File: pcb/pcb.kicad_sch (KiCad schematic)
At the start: 7 parts

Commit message: Start schematic
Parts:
- removed C? (x2): 100n, Capacitor_SMD:C_0603_1608Metric, symbol Device:C
- removed C? (x2): 22u, Capacitor_SMD:CP_Elec_4x3.9, symbol Device:C_Polarized_Small
- removed J?: EURO_PWR_2x5, Connector_IDC:IDC-Header_2x05_P2.54mm_Vertical, symbol eurocad:EURO_PWR_2x5
- removed R? (x2): 22R, Resistor_SMD:R_0603_1608Metric, symbol Device:R
- added C10, C12, C4, C5, C9: 100n, Capacitor_SMD:C_0603_1608Metric, symbol Device:C
- added C11, C13, C2, C3, C6: 10u, Capacitor_SMD:C_0805_2012Metric, symbol Device:C
- added C14, C16: 1n, Capacitor_SMD:C_0603_1608Metric, symbol Device:C
- added C15, C17: 100p, Capacitor_SMD:C_0603_1608Metric, symbol Device:C
- added C7, C8: 2.2u, Capacitor_SMD:C_0805_2012Metric, symbol Device:C
- added D1, D2: 1N5819, Diode_SMD:D_SOD-123, symbol Diode:1N5819
- added D10, D11, D12, D13, D14, D15, D16, D17, D18, D3, D4, D5, D6, D7, D8, D9: BAT54J, Diode_SMD:D_SOD-323F, symbol Diode:BAT54J
- added FB1: BLM21PG600SN1D, Inductor_SMD:L_0805_2012Metric, symbol Device:FerriteBead
- added J1, J10, J11, J2, J3, J5, J6, J7, J8, J9: PJ301M-12, Eurocad:PJ301M-12, symbol eurocad:PJ301M-12
- added J4: EURO_PWR_2x5, Eurocad:Eurorack_Power_Header, symbol eurocad:EURO_PWR_2x5
- added R10, R12, R14, R16, R18, R20, R6, R8: 100K, Resistor_SMD:R_0603_1608Metric, symbol Device:R
- added R11, R13, R15, R17, R19, R21, R25, R29, R7, R9: 1K, Resistor_SMD:R_0603_1608Metric, symbol Device:R
- added R22, R26: 2K2, Resistor_SMD:R_0603_1608Metric, symbol Device:R
- added R23, R27: 10K, Resistor_SMD:R_0603_1608Metric, symbol Device:R
- added R24, R28: 33K, Resistor_SMD:R_0603_1608Metric, symbol Device:R
- added SW1: RotaryEncoder_Switch, Rotary_Encoder:RotaryEncoder_Bourns_Horizontal_PEC09-2xxxF-Nxxxx, symbol Device:RotaryEncoder_Switch
- added U1: PCM5102, Package_SO:TSSOP-20_4.4x6.5mm_P0.65mm, symbol Audio:PCM5102
- added U2: TL072, Package_SO:SOIC-8_3.9x4.9mm_P1.27mm, symbol Amplifier_Operational:TL072
- added U6: Pico, MCU_RaspberryPi_and_Boards:RPi_Pico_SMD_TH, symbol MCU_RaspberryPi_and_Boards:Pico
- added U7: AZ1117-5.0, Package_TO_SOT_SMD:SOT-223-3_TabPin2, symbol Regulator_Linear:AZ1117-5.0
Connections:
- net +12V: now also C2.1, C4.1, D1.1 (K), U2.8 (V+), U7.3 (VI)
- net -12V: now also C3.2, C5.2, D2.2 (A), U2.4 (V-)
- net GND: now also C10.2, C11.2, C12.2, C13.2, C14.2, C16.2, C2.2, C3.1, C4.2, C5.1, C6.2, C8.2, C9.2, D10.2 (A), D12.2 (A), D14.2 (A), D16.2 (A), D18.2 (A), D3.2 (A), D6.2 (A), D8.2 (A), J1.1, J10.1, J11.1, J2.1, J3.1, J4.3 (GND), J4.4 (GND), J4.5 (GND), J4.6 (GND), J4.7 (GND), J4.8 (GND), J5.1, J6.1, J7.1, J8.1, J9.1, R10.1, R12.1, R14.1, R16.1, R18.1, R20.1, R6.1, R8.1, U1.10 (DEMP), U1.11 (FLT), U1.12 (SCK), U1.16 (FMT), U1.19 (DGND), U1.3 (CPGND), U1.9 (AGND), U2.3 (+), U2.5 (+), U6.13 (GND), U6.18 (GND), U6.23 (GND), U6.28 (GND), U6.3 (GND), U6.33 (AGND), U6.38 (GND), U6.42 (GND), U6.8 (GND), U7.1 (GND)
- new net: J2.3, R8.2, R9.2
- new net: C7.1, U1.2 (CAPP)
- new net: C7.2, U1.4 (CAPM)
- new net: C10.1, C11.1, FB1.2, U1.1 (CPVDD), U1.8 (AVDD)
- new net: J8.3, R18.2, R19.2
- new net: J7.3, R16.2, R17.2
- new net: C17.1, R27.1, R28.2, U2.6 (-)
- new net: C17.2, R28.1, R29.2, U2.7
- new net: C9.1, U1.18 (LDOO)
- new net: C8.1, U1.5 (VNEG)
- new net: J6.3, R14.2, R15.2
- new net: J3.3, R10.2, R11.2
- new net: J9.3, R20.2, R21.2
- new net: D1.2 (A), J4.1 (+12V), J4.2 (+12V)
- new net: D2.1 (K), J4.10 (-12V), J4.9 (-12V)
- new net: J5.3, R12.2, R13.2
- new net: C15.2, R24.1, R25.2, U2.1
- new net: C15.1, R23.1, R24.2, U2.2 (-)
- new net: C14.1, R22.1, R23.2
- new net: J11.3, R29.1
- new net: J10.3, R25.1
- new net: C16.1, R26.1, R27.2
- new net: J1.3, R6.2, R7.2
- new net +3V3: C12.1, C13.1, D11.1 (K), D13.1 (K), D15.1 (K), D17.1 (K), D4.1 (K), D5.1 (K), D7.1 (K), D9.1 (K), FB1.1, U1.20 (DVDD), U6.36 (3V3)
- new net +5V: C6.1, U6.39 (VSYS), U7.2 (VO)
- new net GPIO26: U1.14 (DIN), U6.31 (GPIO26_ADC0)
- new net GPIO27: U1.13 (BCK), U6.32 (GPIO27_ADC1)
- new net GPIO28: U1.15 (LRCK), U6.34 (GPIO28_ADC2)
- new net L: R22.2, U1.6 (OUTL)
- new net R: R26.2, U1.7 (OUTR)
- new net TRIGGER 1: D3.1 (K), D4.2 (A), R7.1
- new net TRIGGER 2: D5.2 (A), D6.1 (K), R9.1
- new net TRIGGER 3: D7.2 (A), D8.1 (K), R11.1
- new net TRIGGER 4: D10.1 (K), D9.2 (A), R13.1
- new net TRIGGER 5: D11.2 (A), D12.1 (K), R15.1
- new net TRIGGER 6: D13.2 (A), D14.1 (K), R17.1
- new net TRIGGER 7: D15.2 (A), D16.1 (K), R19.1
- new net TRIGGER 8: D17.2 (A), D18.1 (K), R21.1
- no-connect marks 0 -> 10

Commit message: Continue schematic
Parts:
- added R30, R31, R32: 100K, Resistor_SMD:R_0603_1608Metric, symbol Device:R
- SW1: value RotaryEncoder_Switch -> Encoder
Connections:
- net +3V3: now also R30.2, R31.2, R32.2
- net GND: now also SW1.C, SW1.S2
- net GPIO26: no longer U1.14 (DIN)
- net GPIO27: no longer U1.13 (BCK)
- net GPIO28: now also SW1.S1, R30.1; no longer U1.15 (LRCK)
- net GPIO18: now reaches U6.24 (GPIO18)
- net GPIO18: now also SW1.A, R31.1
- net GPIO19: now reaches U6.25 (GPIO19)
- net GPIO19: now also SW1.B, R32.1
- net GPIO20: now reaches U6.26 (GPIO20)
- net GPIO20: now also U1.14 (DIN)
- net GPIO21: now reaches U6.27 (GPIO21)
- net GPIO21: now also U1.13 (BCK)
- net GPIO22: now reaches U6.29 (GPIO22)
- net GPIO22: now also U1.15 (LRCK)
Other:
- moved on the sheet: SW1

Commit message: Add LEDs, Triggers and CV in (closes #1)
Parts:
- added D19, D20, D21, D22, D23, D24, D25, D26: 3mm LED Com. Cath., LED_THT:LED_D3.0mm-3, symbol Device:LED_Dual_AKA
- added J12: PJ301M-12, Eurocad:PJ301M-12, symbol eurocad:PJ301M-12
- added Q1, Q2, Q3, Q4, Q5, Q6, Q7, Q8: MMBT3906, Package_TO_SOT_SMD:SOT-23, symbol Transistor_BJT:MMBT3906
- added R33, R36, R39, R40, R45, R46, R47, R48: 1K, Resistor_SMD:R_0603_1608Metric, symbol Device:R
- added R34, R35, R37, R38, R41, R42, R43, R44, R49, R50, R51, R52, R53, R54, R55, R56: 330R, Resistor_SMD:R_0603_1608Metric, symbol Device:R
- added R57, R59, R61: 100K, Resistor_SMD:R_0603_1608Metric, symbol Device:R
- added R58: 15K, Resistor_SMD:R_0603_1608Metric, symbol Device:R
- added R60: 12K, Resistor_SMD:R_0603_1608Metric, symbol Device:R
- added U3: MCP6002-xSN, Package_SO:SOIC-8_3.9x4.9mm_P1.27mm, symbol Amplifier_Operational:MCP6002-xSN
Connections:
- net +12V: now also U3.8 (V+)
- net +3V3: now also Q1.2 (E), Q2.2 (E), Q3.2 (E), Q4.2 (E), Q5.2 (E), Q6.2 (E), Q7.2 (E), Q8.2 (E)
- net -12V: now also R60.2, U3.4 (V-)
- net GND: now also D19.2 (K), D20.2 (K), D21.2 (K), D22.2 (K), D23.2 (K), D24.2 (K), D25.2 (K), D26.2 (K), J12.1, J12.2, R61.2, U3.3 (+), U3.5 (+)
- net TRIGGER 1: now also U6.1 (GPIO0)
- net TRIGGER 2: now also U6.4 (GPIO2)
- net TRIGGER 3: now also U6.6 (GPIO4)
- net TRIGGER 4: now also U6.9 (GPIO6)
- net TRIGGER 5: now also U6.11 (GPIO8)
- net TRIGGER 6: now also U6.14 (GPIO10)
- net TRIGGER 7: now also U6.16 (GPIO12)
- net TRIGGER 8: now also U6.19 (GPIO14)
- net LED 4: now reaches U6.10 (GPIO7)
- net LED 4: now also R39.2, R42.2
- net LED 5: now reaches U6.12 (GPIO9)
- net LED 5: now also R48.2, R56.2
- net LED 6: now reaches U6.15 (GPIO11)
- net LED 6: now also R47.2, R54.2
- net LED 7: now reaches U6.17 (GPIO13)
- net LED 7: now also R46.2, R52.2
- net LED 1: now reaches U6.2 (GPIO1)
- net LED 1: now also R33.2, R35.2
- net LED 8: now reaches U6.20 (GPIO15)
- net LED 8: now also R45.2, R50.2
- net LED 2: now reaches U6.5 (GPIO3)
- net LED 2: now also R36.2, R38.2
- net LED 3: now reaches U6.7 (GPIO5)
- net LED 3: now also R40.2, R44.2
- net GPIO26 renamed CV
- net CV: now also R58.1, U3.1
- net GPIO27: no longer names the net of U6.32 (GPIO27_ADC1)
- new net: D23.1 (A1), R50.1
- new net: D23.3 (A2), R49.2
- new net: Q3.1 (B), R39.1
- new net: Q3.3 (C), R41.1
- new net: Q1.3 (C), R34.1
- new net: D19.3 (A2), R34.2
- new net: Q8.1 (B), R48.1
- new net: D21.1 (A1), R42.1
- new net: D21.3 (A2), R41.2
- new net: Q6.1 (B), R46.1
- new net: Q6.3 (C), R51.1
- new net: D20.1 (A1), R38.1
- new net: D20.3 (A2), R37.2
- new net: D26.1 (A1), R56.1
- new net: Q8.3 (C), R55.1
- new net: D26.3 (A2), R55.2
- new net: D22.1 (A1), R44.1
- new net: D22.3 (A2), R43.2
- new net: Q1.1 (B), R33.1
- new net: Q5.3 (C), R49.1
- new net: D25.1 (A1), R54.1
- new net: D25.3 (A2), R53.2
- new net: U3.6 (-), U3.7
- new net: Q2.1 (B), R36.1
- new net: Q2.3 (C), R37.1
- new net: D24.1 (A1), R52.1
- new net: Q4.1 (B), R40.1
- new net: D19.1 (A1), R35.1
- new net: Q5.1 (B), R45.1
- new net: Q7.1 (B), R47.1
- new net: D24.3 (A2), R51.2
- new net: Q7.3 (C), R53.1
- new net: R57.1, R58.2, R59.1, U3.2 (-)
- new net: J12.3, R57.2
- new net: Q4.3 (C), R43.1
- new net -10V: R59.2, R60.1, R61.1
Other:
- moved on the sheet: C14, C15, C16, C17, C2, C3, C4, C5, C6, D1, D2, J10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

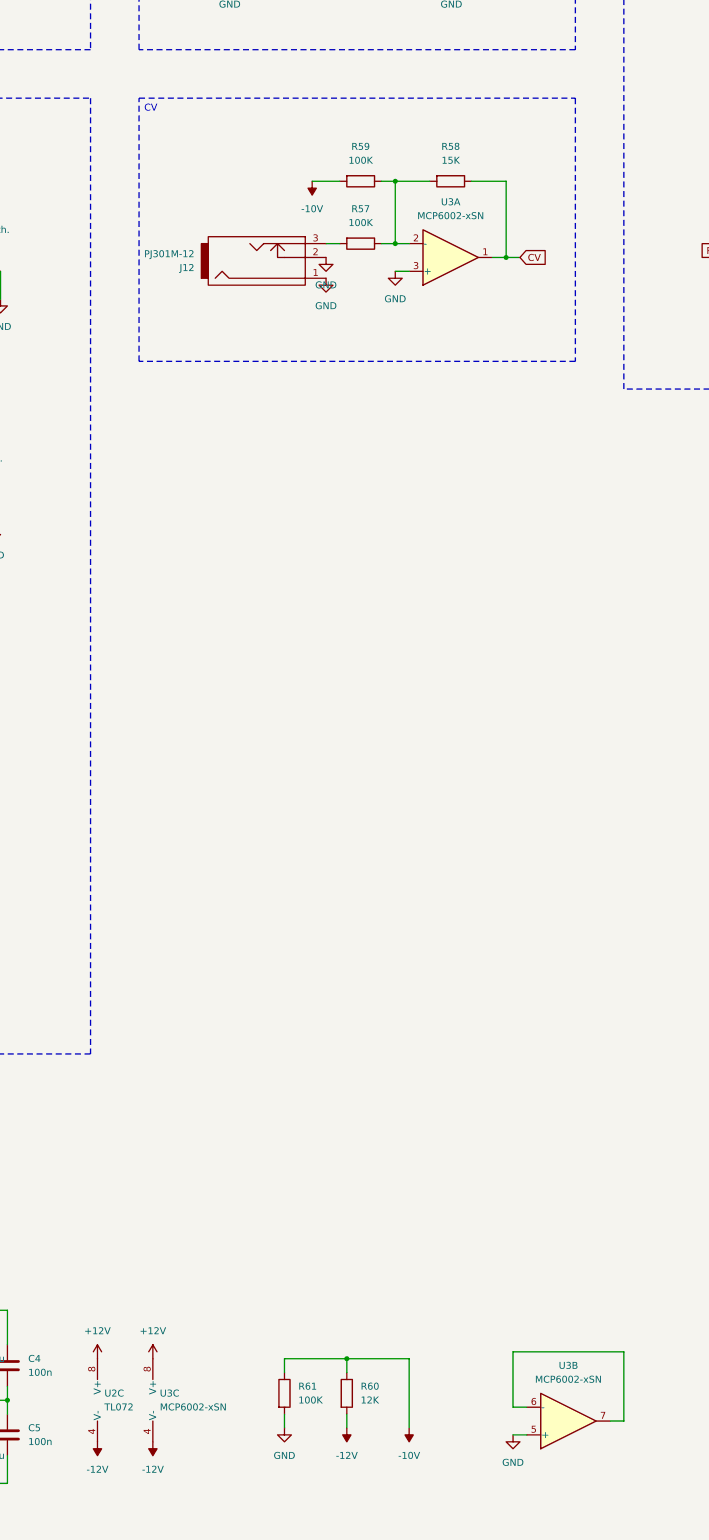
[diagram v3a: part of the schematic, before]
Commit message: Replace OP-Amp and add GPIO input protection diodes for eventual clamping
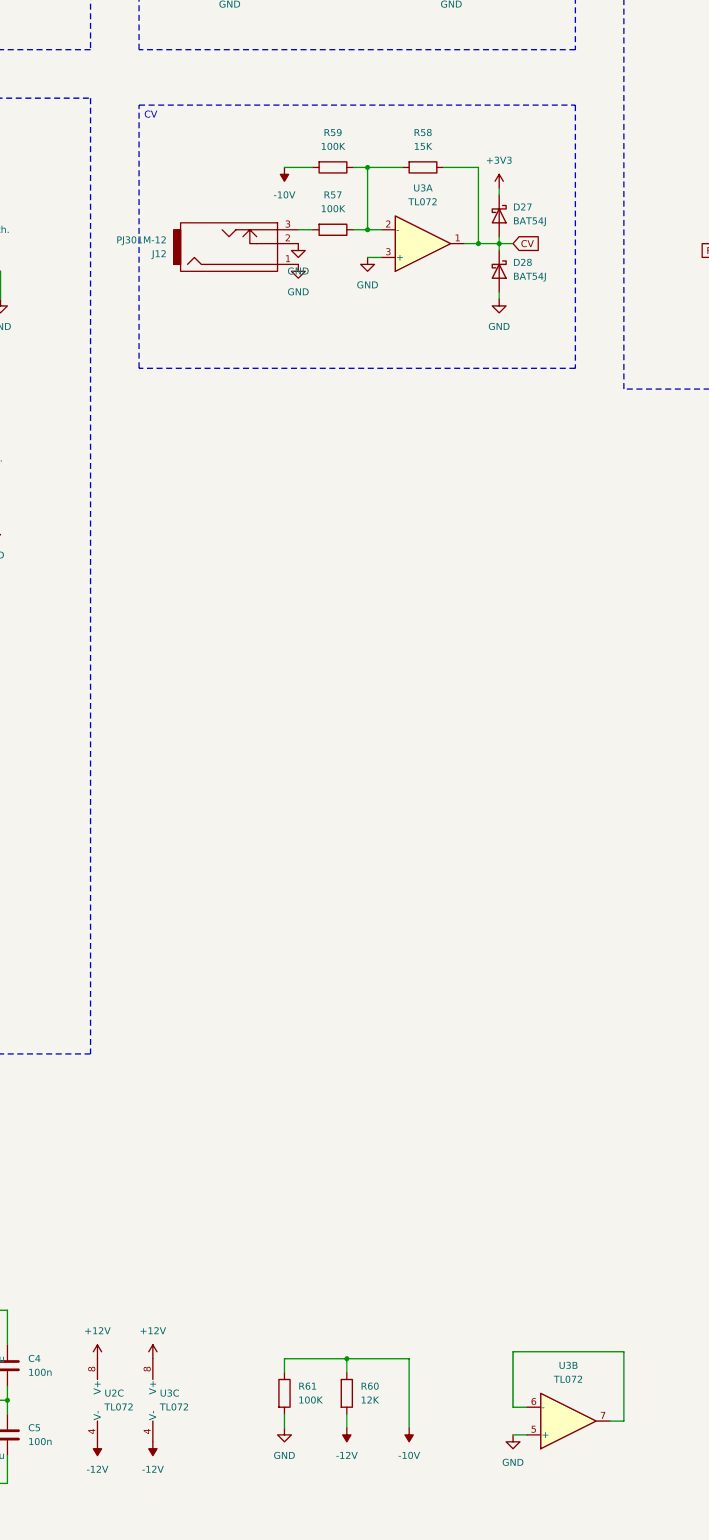
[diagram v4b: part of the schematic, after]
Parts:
- removed U3: MCP6002-xSN, Package_SO:SOIC-8_3.9x4.9mm_P1.27mm, symbol Amplifier_Operational:MCP6002-xSN
- added D27, D28: BAT54J, Diode_SMD:D_SOD-323F, symbol Diode:BAT54J
- added U3: TL072, Package_SO:SOIC-8_3.9x4.9mm_P1.27mm, symbol Amplifier_Operational:TL072
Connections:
- net +12V: now also U3.8 (V+)
- net +3V3: now also D27.1 (K)
- net -12V: now also U3.4 (V-)
- net CV: now also D27.2 (A), D28.1 (K), U3.1
- net GND: now also D28.2 (A), U3.3 (+), U3.5 (+)
- net at R57.1, R58.2, R59.1: now also U3.2 (-)
- new net: U3.6 (-), U3.7
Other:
- moved on the sheet: J12, R57, R58, R59

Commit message: Implement feedback from Niek
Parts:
- removed D10, D11, D12, D13, D14, D15, D16, D17, D18, D27, D28, D3, D4, D5, D6, D7, D8, D9: BAT54J, Diode_SMD:D_SOD-323F, symbol Diode:BAT54J
- added C18, C19, C20: 100n, Capacitor_SMD:C_0603_1608Metric, symbol Device:C
- added D29, D30, D31, D32, D33, D34, D35, D36, D37: BAT54S, Package_TO_SOT_SMD:SOT-23, symbol Diode:BAT54S
- R57: value 100K -> 50K
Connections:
- net +12V: now also C18.1
- net +3V3: now also D29.2 (K), D30.2 (K), D31.2 (K), D32.2 (K), D33.2 (K), D34.2 (K), D35.2 (K), D36.2 (K), D37.2 (K)
- net -10V: now also U3.6 (-), U3.7; no longer R60.1, R61.1
- net -12V: now also C19.2
- net CV: now also D37.3 (COM)
- net GND: now also C18.2, C19.1, C20.2, D29.1 (A), D30.1 (A), D31.1 (A), D32.1 (A), D33.1 (A), D34.1 (A), D35.1 (A), D36.1 (A), D37.1 (A); no longer U3.5 (+)
- net GPIO28: now also C20.1
- net TRIGGER 1: now also D29.3 (COM)
- net TRIGGER 2: now also D30.3 (COM)
- net TRIGGER 3: now also D31.3 (COM)
- net TRIGGER 4: now also D32.3 (COM)
- net TRIGGER 5: now also D36.3 (COM)
- net TRIGGER 6: now also D35.3 (COM)
- net TRIGGER 7: now also D34.3 (COM)
- net TRIGGER 8: now also D33.3 (COM)
- new net: R60.1, R61.1, U3.5 (+)
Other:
- moved on the sheet: J1, J12, J2, J3, J5, J6, J7, J8, J9, R10, R11, R12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

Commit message: Rev 1
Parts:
- added D3: LED, LED_SMD:LED_0603_1608Metric, symbol Device:LED
- added R62: 2K, Resistor_SMD:R_0603_1608Metric, symbol Device:R
- SW1: footprint Rotary_Encoder:RotaryEncoder_Bourns_Horizontal_PEC09-2xxxF-Nxxxx -> Rotary_Encoder:RotaryEncoder_Alps_EC11E-Switch_Vertical_H20mm
- U6: footprint MCU_RaspberryPi_and_Boards:RPi_Pico_SMD_TH -> Module:RaspberryPi_Pico_Common_THT
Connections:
- net +12V: now also R62.1
- net GND: now also D3.1 (K)
- new net: D3.2 (A), R62.2

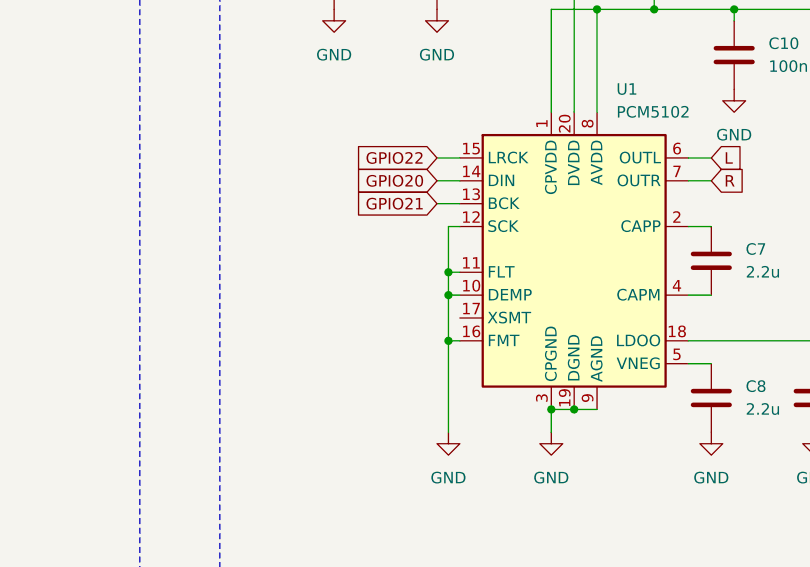
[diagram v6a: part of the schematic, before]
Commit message: Fix missing XSMT connection to 3V3
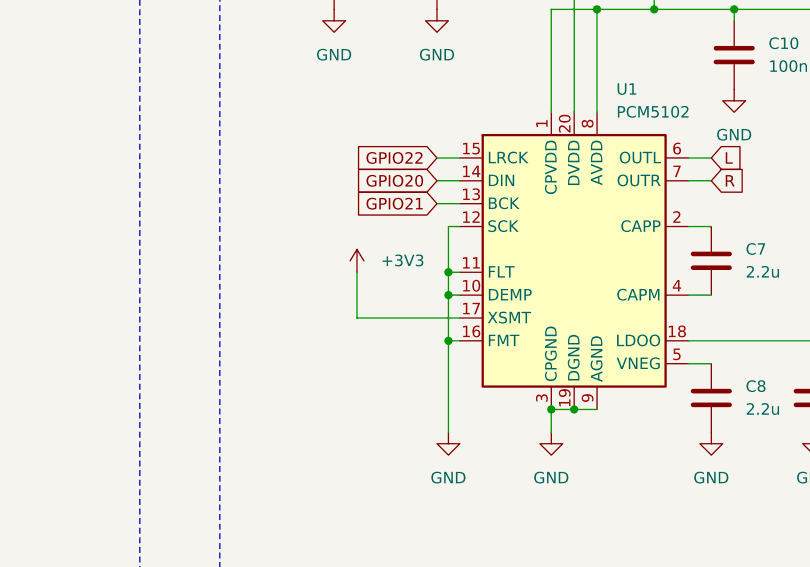
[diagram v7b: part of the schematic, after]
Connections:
- net +3V3: now also U1.17 (XSMT)
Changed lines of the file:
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@@
 	(wire
 		(pts
+			(xy 208.28 86.36) (xy 208.28 81.28)
+		)
+		(stroke
+			(width 0)
+			(type default)
+		)
+	)
+	(wire
+		(pts
 			(xy 125.73 359.41) (xy 121.92 359.41)
 		)
@@
 	(wire
 		(pts
+			(xy 219.71 86.36) (xy 208.28 86.36)
+		)
+		(stroke
+			(width 0)
+			(type default)
+		)
+	)
+	(wire
+		(pts
 			(xy 218.44 81.28) (xy 219.71 81.28)
 		)
@@
 					(unit 1)
 				)
+			)
+		)
+	)
+	(symbol
+		(lib_id "power:+3.3V")
+		(at 208.28 81.28 0)
+		(unit 1)
+		(exclude_from_sim no)
+		(in_bom yes)
+		(on_board yes)
+		(dnp no)
+		(property "Reference" "#PWR093"
+			(at 208.28 85.09 0)
+			(effects
+				(font
+					(size 1.27 1.27)
+				)
+				(hide yes)
+			)
+		)
+		(property "Value" "+3V3"
+			(at 213.36 80.01 0)
+			(effects
+				(font
+					(size 1.27 1.27)
+				)
+			)
+		)
+		(property "Footprint" ""
+			(at 208.28 81.28 0)
+			(effects
+				(font
+					(size 1.27 1.27)
+				)
+				(hide yes)
+			)
+		)
+		(property "Datasheet" ""
+			(at 208.28 81.28 0)
+			(effects
+				(font
+					(size 1.27 1.27)
+				)
+				(hide yes)
+			)
+		)
+		(property "Description" ""
+			(at 208.28 81.28 0)
+			(effects
+				(font
+					(size 1.27 1.27)
+				)
+			)
+		)
+		(pin "1"
+		)
+		(instances
+			(project "pcb"
+				(path "/e63e39d7-6ac0-4ffd-8aa3-1841a4541b55"
+					(reference "#PWR093")
+					(unit 1)
+				)

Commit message: Fix 3V3 missing on DAC and use additional LDO for 3V3 on DAC
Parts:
- removed FB1: BLM21PG600SN1D, Inductor_SMD:L_0805_2012Metric, symbol Device:FerriteBead
- added C21: 2u2, Capacitor_SMD:C_0805_2012Metric, symbol Device:C
- added C22: 1u, Capacitor_SMD:C_0805_2012Metric, symbol Device:C
- added U4: LD2981ABM33TR, Package_TO_SOT_SMD:SOT-23-5, symbol Regulator_Linear:LP2985-3.3
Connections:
- net +12V: now also C22.1, U4.1 (VIN), U4.3 (ON/~{OFF})
- net GND: now also C21.2, C22.2, U4.2 (GND)
- net +3.3VA: now reaches C10.1, C11.1, U1.1 (CPVDD), U1.8 (AVDD)
- net +3.3VA: now also C21.1, U4.5 (VOUT)
- no-connect marks 10 -> 11
